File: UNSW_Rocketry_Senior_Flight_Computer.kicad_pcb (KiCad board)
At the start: 4 copper layers, 60 x 60 mm, 132 parts, among them J1 BATT_XT60, J2 Micro_SD_Card_Det1, J3 USB_C_Receptacle_USB2.0_16P, J4 SWD, J5 Conn_01x04, J6 PYRO_XT60, J7 J_PYRO1, J8 J_PYRO2, Q1 DMG2301L, Q2 AO3401A, Q3 AO3400A, Q4 AO3400A, Q5 AO3400A, U1 STM32L452RETx, U10 PC817, U11 PC817, U2 TPS63060, U3 SPX3819M5-L-3-3, U4 H3LIS331DL, U5 MS5611 #1, U6 LIS3DH, U7 MS5611 #2, U8 USBLC6-2SC6, U9 PC817, Y1 8MHz

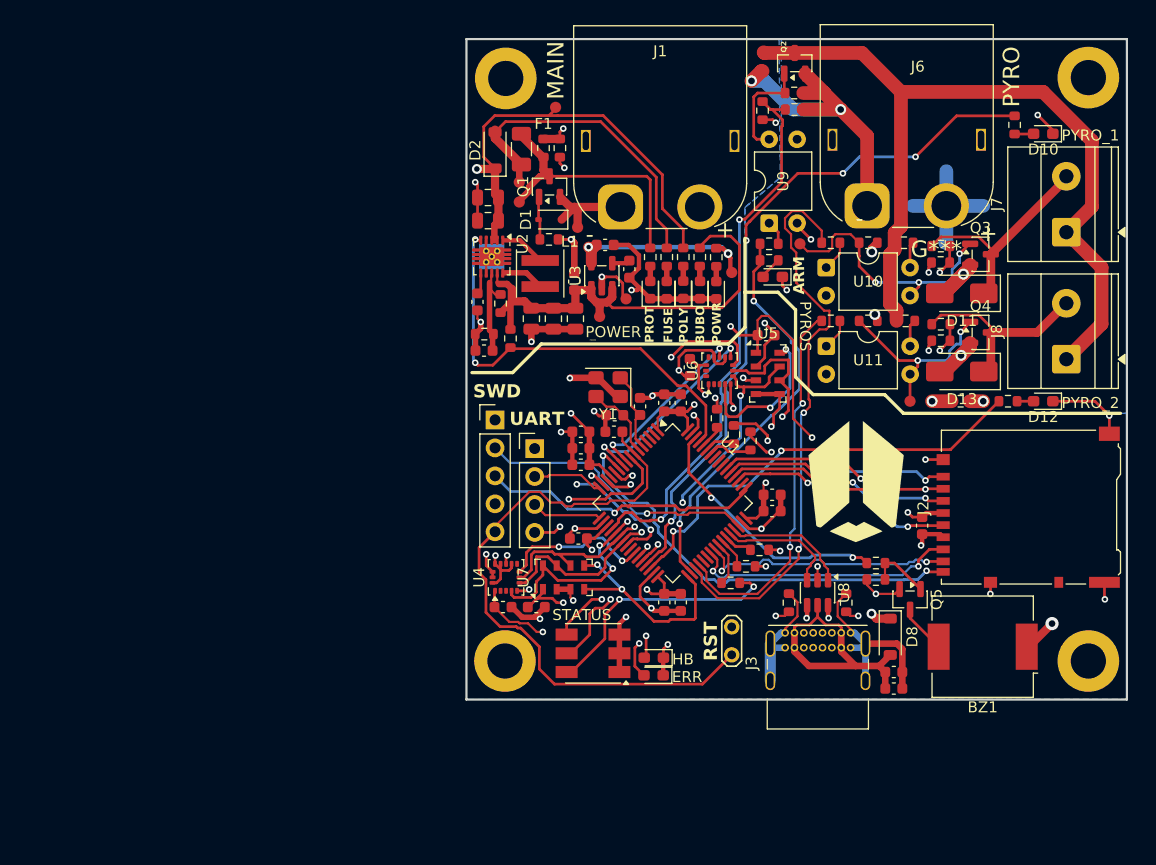
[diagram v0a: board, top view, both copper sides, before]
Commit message: chore: save working flight computer state as v0.0 baseline
Final known-good state of the senior FC before splitting into versioned
revisions (v0.0 frozen, v1.0 for the next revision).

Co-Authored-By: Claude Opus 4.7 (1M context) <noreply@anthropic.com>
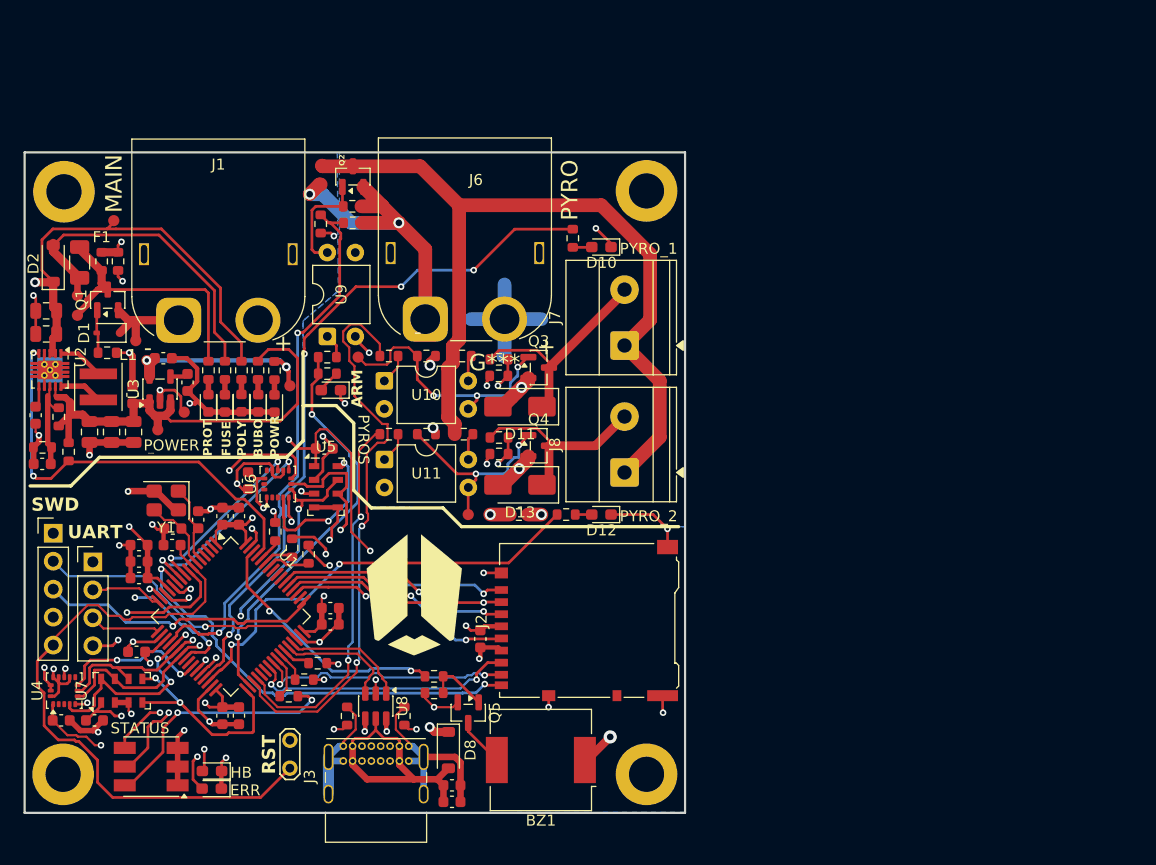
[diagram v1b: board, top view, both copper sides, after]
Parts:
- moved BZ1 41.4 mm to (167.3, 125.0)
- moved C1 41.4 mm to (133.8, 104.0)
- moved C11 41.4 mm to (139.8, 102.8)
- moved C12 41.4 mm to (139.8, 121.0)
- moved C13 41.4 mm to (138.3, 121.0)
- moved C24 41.4 mm to (161.8, 114.0)
- moved C28 41.4 mm to (140.7, 99.6)
- moved C6 41.4 mm to (138.3, 102.8)
- moved D10 41.4 mm to (172.8, 78.4)
- moved D16 41.4 mm to (137.4, 126.0)
- moved G*** 41.4 mm to (155.8, 110.0)
- moved R13 41.4 mm to (149.7, 121.0)
- moved R16 41.4 mm to (147.3, 76.3)
- moved R24 41.4 mm to (170.2, 77.6)
- moved R28 41.4 mm to (160.3, 95.4)
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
